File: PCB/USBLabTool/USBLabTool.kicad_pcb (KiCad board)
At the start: 2 copper layers, 228 parts, among them J1 Conn_01x06_Pin, J10 T_pwm, J11 T_buf, J12 T_buf, J13 ADC2, J14 ADC1, J15 +3.3VA, J16 +3.3VA, J17 2x01, J19 T_N5V, J2 Conn_02x12_Odd_Even, J20 USB_C_Receptacle, J3 T_att, J4 T_att, J5 T_acdc, J6 T_acdc, J7 T_amp, J8 T_amp, J9 T_pwm, K1 G5V-2, K2 G5V-2, SW1 SW_Push, U1 AQY284SX, U10 Opamp_Quad, U11 DG403, U12 STM32H562VGTx, U13 r1283, U14 ST1L05APU33R, U15 ST1L05APU33R, U16 LTC1983ES6-5#TRPBF, U17 TCPP01-M12, U18 74HC245, U2 AQY284SX, U20 74HC245, U3 CD74HC4316M96, U4 LMP7718, U5 CD74HC4316M96, U6 LMP7718, U7 OPA863, U8 OPA863, U9 Opamp_Quad, Y1 32.768kHz

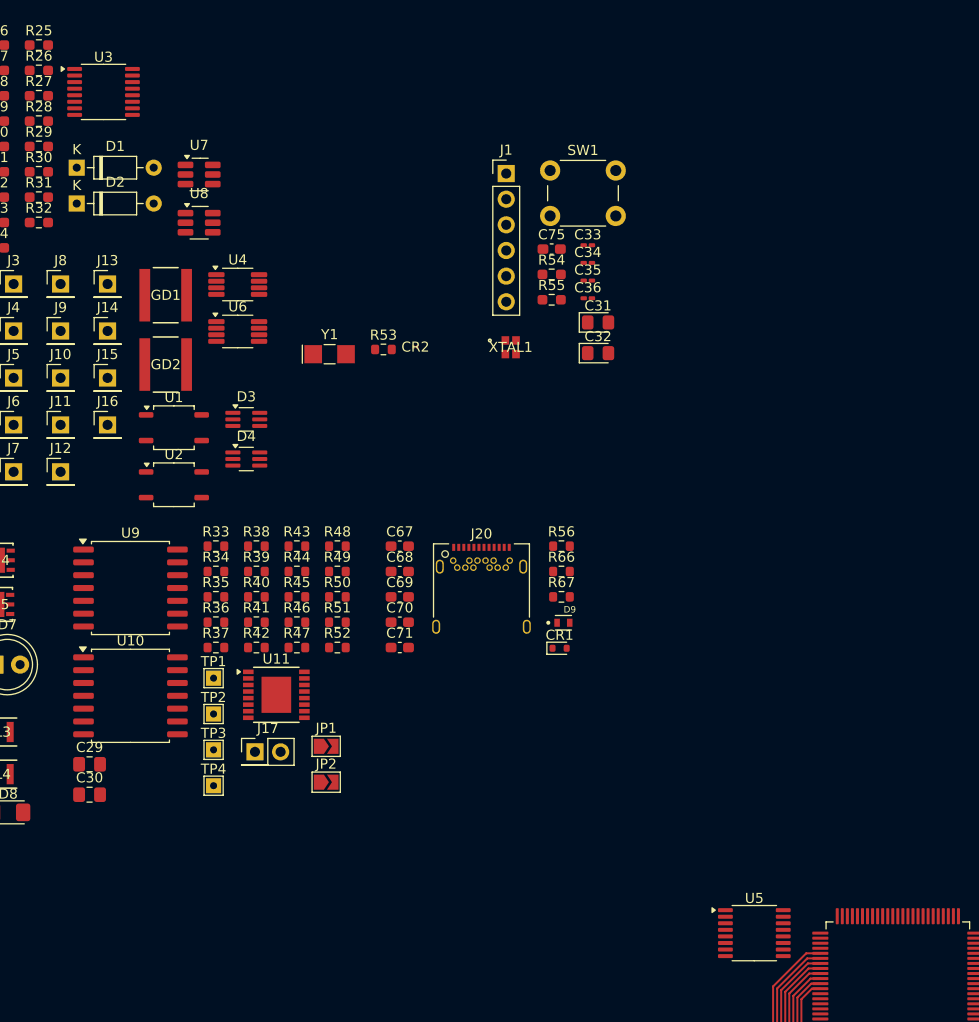
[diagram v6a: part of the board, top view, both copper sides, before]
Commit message: swap MCU  pins for routing
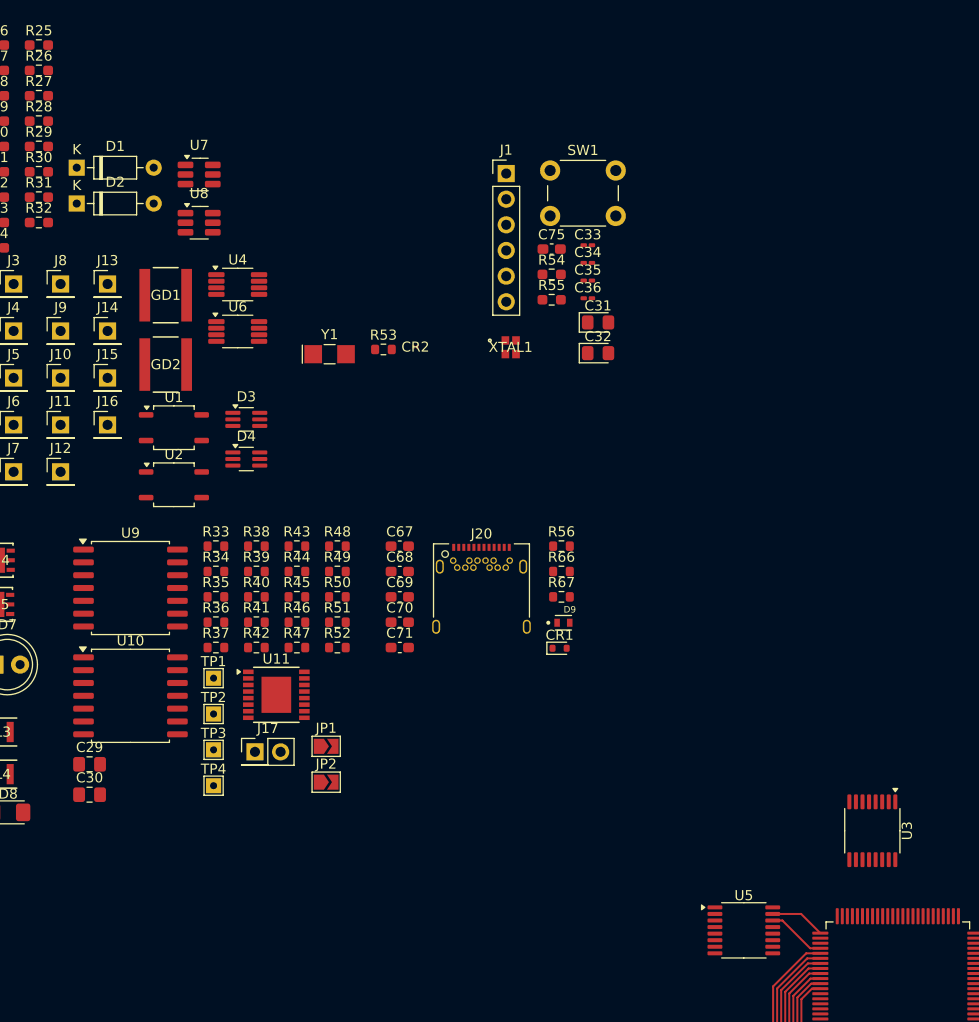
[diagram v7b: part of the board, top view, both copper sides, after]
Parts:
- U3, U5: value CD74HC4316M96 -> CD74HC4316PWR
- moved U3 105.6 mm to (140.6, 105.3), turned to -90 degrees
- moved U5 1.07 mm to (127.9, 115.2)
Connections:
- U12 pad 35: CH1_amp_10 -> CH1_amp_1
- U12 pad 47: CH1_amp_1 -> CH1_amp_10
- U12 pad 51: CH0_amp_10 -> CH0_amp_1
- U12 pad 54: CH0_amp_1 -> CH0_amp_10
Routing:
- net CH0_amp_10: track 0.00 -> 5.85 mm
- net CH0_amp_1: track 0.00 -> 5.50 mm
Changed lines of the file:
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@@
 			(layers "F.Cu" "F.Paste" "F.Mask")
 			(roundrect_rratio 0.25)
-			(net 139 "CH1_amp_10")
+			(net 141 "CH1_amp_1")
 			(pinfunction "PB0")
 			(pintype "bidirectional")
@@
 			(layers "F.Cu" "F.Paste" "F.Mask")
 			(roundrect_rratio 0.25)
-			(net 141 "CH1_amp_1")
+			(net 139 "CH1_amp_10")
 			(pinfunction "PB10")
 			(pintype "bidirectional")
@@
 			(layers "F.Cu" "F.Paste" "F.Mask")
 			(roundrect_rratio 0.25)
-			(net 146 "CH0_amp_10")
+			(net 143 "CH0_amp_1")
 			(pinfunction "PB12")
 			(pintype "bidirectional")
@@
 			(layers "F.Cu" "F.Paste" "F.Mask")
 			(roundrect_rratio 0.25)
-			(net 143 "CH0_amp_1")
+			(net 146 "CH0_amp_10")
 			(pinfunction "PB15")
 			(pintype "bidirectional")
@@
 	(footprint "Package_SO:TSSOP-16_4.4x5mm_P0.65mm"
 		(layer "F.Cu")
-		(at 128.9375 115.475)
+		(at 127.9 115.2)
 		(descr "TSSOP, 16 Pin (https://www.jedec.org/document_search?search_api_views_fulltext=MO-153), generated with kicad-footprint-generator ipc_gullwing_generator.py")
 		(tags "TSSOP SO JEDEC-MO-153-AB TI-PW0016A Microchip-ST Toshiba-TSSOP16-P-0044-0.65A NXP-SOT403-1 Infineon-P-TSSOP-16-800")
@@
 			)
 		)
-		(property "Value" "CD74HC4316M96"
+		(property "Value" "CD74HC4316PWR"
 			(at 0 3.45 0)
 			(layer "F.Fab")
@@
 			)
 		)
-		(property "Datasheet" "https://www.digikey.com/en/products/detail/texas-instruments/CD74HC4316M96/555784"
+		(property "Datasheet" "https://www.digikey.com/en/products/detail/texas-instruments/CD74HC4316PWR/1507290"
 			(at 0 0 0)
 			(layer "F.Fab")
@@
 		(fp_text user "*"
 			(at -2.4638 -0.75 0)
-			(unlocked yes)
 			(layer "F.SilkS")
 			(effects
@@
 		(fp_text user "*"
 			(at -2.4638 -0.75 0)
+			(unlocked yes)
 			(layer "F.SilkS")
 			(effects
@@
 		(fp_text user "*"
 			(at -1.016 -0.75 0)
+			(unlocked yes)
 			(layer "F.Fab")
 			(effects
@@
 		(fp_text user "*"
 			(at -1.016 -0.75 0)
-			(unlocked yes)
 			(layer "F.Fab")
 			(effects
@@
 	(footprint "Package_SO:TSSOP-16_4.4x5mm_P0.65mm"
 		(layer "F.Cu")
-		(at 64.49 32.175)
+		(at 140.625 105.3375 -90)
 		(descr "TSSOP, 16 Pin (https://www.jedec.org/document_search?search_api_views_fulltext=MO-153), generated with kicad-footprint-generator ipc_gullwing_generator.py")
 		(tags "TSSOP SO JEDEC-MO-153-AB TI-PW0016A Microchip-ST Toshiba-TSSOP16-P-0044-0.65A NXP-SOT403-1 Infineon-P-TSSOP-16-800")
 		(property "Reference" "U3"
-			(at 0 -3.45 0)
+			(at 0 -3.45 90)
 			(layer "F.SilkS")
 			(effects
@@
 			)
 		)
-		(property "Value" "CD74HC4316M96"
-			(at 0 3.45 0)
+		(property "Value" "CD74HC4316PWR"
+			(at 0 3.45 90)
 			(layer "F.Fab")
 			(effects
@@
 		)
 		(property "Footprint" "Package_SO:TSSOP-16_4.4x5mm_P0.65mm"
-			(at 0 0 0)
+			(at 0 0 90)
 			(layer "F.Fab")
 			(hide yes)
@@
 			)
 		)
-		(property "Datasheet" "https://www.digikey.com/en/products/detail/texas-instruments/CD74HC4316M96/555784"
-			(at 0 0 0)
+		(property "Datasheet" "https://www.digikey.com/en/products/detail/texas-instruments/CD74HC4316PWR/1507290"
+			(at 0 0 90)
 			(layer "F.Fab")
 			(hide yes)
@@
 		)
 		(property "Description" ""
-			(at 0 0 0)
+			(at 0 0 90)
 			(layer "F.Fab")
 			(hide yes)
@@
 		(attr smd)
 		(fp_line
-			(start 0 -2.735)
-			(end -2.2 -2.735)
+			(start 0 2.735)
+			(end -2.2 2.735)
 			(stroke
 				(width 0.12)
@@
 		)
 		(fp_line
-			(start 0 -2.735)
-			(end 2.2 -2.735)
+			(start 0 2.735)
+			(end 2.2 2.735)
 			(stroke
 				(width 0.12)
@@
 		)
 		(fp_line
-			(start 0 2.735)
-			(end -2.2 2.735)
+			(start 0 -2.735)
+			(end -2.2 -2.735)
 			(stroke
 				(width 0.12)
@@
 		)
 		(fp_line
-			(start 0 2.735)
-			(end 2.2 2.735)
+			(start 0 -2.735)
+			(end 2.2 -2.735)
 			(stroke
 				(width 0.12)
@@
 		)
 		(fp_line
-			(start -3.85 -2.75)
-			(end -3.85 2.75)
+			(start -3.85 2.75)
+			(end 3.85 2.75)
 			(stroke
 				(width 0.05)
@@
 		)
 		(fp_line
-			(start -3.85 2.75)
-			(end 3.85 2.75)
+			(start 3.85 2.75)
+			(end 3.85 -2.75)
 			(stroke
 				(width 0.05)
@@
 		)
 		(fp_line
-			(start 3.85 -2.75)
-			(end -3.85 -2.75)
+			(start -3.85 -2.75)
+			(end -3.85 2.75)
 			(stroke
 				(width 0.05)
@@
 		)
 		(fp_line
-			(start 3.85 2.75)
-			(end 3.85 -2.75)
+			(start 3.85 -2.75)
+			(end -3.85 -2.75)
 			(stroke
 				(width 0.05)
@@
 		)
 		(fp_line
-			(start -2.2 -1.5)
-			(end -1.2 -2.5)
+			(start -2.2 2.5)
+			(end -2.2 -1.5)
 			(stroke
 				(width 0.1)
@@
 		)
 		(fp_line
-			(start -2.2 2.5)
-			(end -2.2 -1.5)
+			(start 2.2 2.5)
+			(end -2.2 2.5)
 			(stroke
 				(width 0.1)
@@
 		)
 		(fp_line
-			(start -1.2 -2.5)
-			(end 2.2 -2.5)
+			(start -2.2 -1.5)
+			(end -1.2 -2.5)
 			(stroke
 				(width 0.1)
@@
 		)
 		(fp_line
-			(start 2.2 -2.5)
-			(end 2.2 2.5)
+			(start -1.2 -2.5)
+			(end 2.2 -2.5)
 			(stroke
 				(width 0.1)
@@
 		)
 		(fp_line
-			(start 2.2 2.5)
-			(end -2.2 2.5)
+			(start 2.2 -2.5)
+			(end 2.2 2.5)
 			(stroke
 				(width 0.1)
@@
 		)
 		(fp_text user "${REFERENCE}"
-			(at 0 0 0)
+			(at 0 0 90)
 			(layer "F.Fab")
 			(effects
@@
 		)
 		(pad "1" smd roundrect
-			(at -2.8625 -2.275)
+			(at -2.8625 -2.275 270)
 			(size 1.475 0.4)
 			(layers "F.Cu" "F.Paste" "F.Mask")
@@
 		)
 		(pad "2" smd roundrect
-			(at -2.8625 -1.625)
+			(at -2.8625 -1.625 270)
 			(size 1.475 0.4)
 			(layers "F.Cu" "F.Paste" "F.Mask")
@@
 		)
 		(pad "3" smd roundrect
-			(at -2.8625 -0.975)
+			(at -2.8625 -0.975 270)
 			(size 1.475 0.4)
 			(layers "F.Cu" "F.Paste" "F.Mask")
@@
 		)
 		(pad "4" smd roundrect
-			(at -2.8625 -0.325)
+			(at -2.8625 -0.325 270)
 			(size 1.475 0.4)
 			(layers "F.Cu" "F.Paste" "F.Mask")
@@
 		)
 		(pad "5" smd roundrect
-			(at -2.8625 0.325)
+			(at -2.8625 0.325 270)
 			(size 1.475 0.4)
 			(layers "F.Cu" "F.Paste" "F.Mask")
@@
 		)
 		(pad "6" smd roundrect
-			(at -2.8625 0.975)
+			(at -2.8625 0.975 270)
 			(size 1.475 0.4)
 			(layers "F.Cu" "F.Paste" "F.Mask")
@@
 		)
 		(pad "7" smd roundrect
-			(at -2.8625 1.625)
+			(at -2.8625 1.625 270)
 			(size 1.475 0.4)
 			(layers "F.Cu" "F.Paste" "F.Mask")
@@
 		)
 		(pad "8" smd roundrect
-			(at -2.8625 2.275)
+			(at -2.8625 2.275 270)
 			(size 1.475 0.4)
 			(layers "F.Cu" "F.Paste" "F.Mask")
@@
 		)
 		(pad "9" smd roundrect
-			(at 2.8625 2.275)
+			(at 2.8625 2.275 270)
 			(size 1.475 0.4)
 			(layers "F.Cu" "F.Paste" "F.Mask")
@@
 		)
 		(pad "10" smd roundrect
-			(at 2.8625 1.625)
+			(at 2.8625 1.625 270)
 			(size 1.475 0.4)
 			(layers "F.Cu" "F.Paste" "F.Mask")
@@
 		)
 		(pad "11" smd roundrect
-			(at 2.8625 0.975)
+			(at 2.8625 0.975 270)
 			(size 1.475 0.4)
 			(layers "F.Cu" "F.Paste" "F.Mask")
@@
 		)
 		(pad "12" smd roundrect
-			(at 2.8625 0.325)
+			(at 2.8625 0.325 270)
 			(size 1.475 0.4)
 			(layers "F.Cu" "F.Paste" "F.Mask")
@@
 		)
 		(pad "13" smd roundrect
-			(at 2.8625 -0.325)
+			(at 2.8625 -0.325 270)
 			(size 1.475 0.4)
 			(layers "F.Cu" "F.Paste" "F.Mask")
@@
 		)
 		(pad "14" smd roundrect
-			(at 2.8625 -0.975)
+			(at 2.8625 -0.975 270)
 			(size 1.475 0.4)
 			(layers "F.Cu" "F.Paste" "F.Mask")
@@
 		)
 		(pad "15" smd roundrect
-			(at 2.8625 -1.625)
+			(at 2.8625 -1.625 270)
 			(size 1.475 0.4)
 			(layers "F.Cu" "F.Paste" "F.Mask")
@@
 		)
 		(pad "16" smd roundrect
-			(at 2.8625 -2.275)
+			(at 2.8625 -2.275 270)
 			(size 1.475 0.4)
 			(layers "F.Cu" "F.Paste" "F.Mask")
@@
 	)
 	(segment
+		(start 130.7625 113.575)
+		(end 133.575 113.575)
+		(width 0.2)
+		(layer "F.Cu")
+		(net 143)
+	)
+	(segment
+		(start 133.575 113.575)
+		(end 135.475 115.475)
+		(width 0.2)
+		(layer "F.Cu")
+		(net 143)
+	)
+	(segment
+		(start 134.468456 116.975)
+		(end 135.475 116.975)
+		(width 0.2)
+		(layer "F.Cu")
+		(net 146)
+	)
+	(segment
+		(start 130.7625 114.225)
+		(end 131.718456 114.225)
+		(width 0.2)
+		(layer "F.Cu")
+		(net 146)
+	)
+	(segment
+		(start 131.718456 114.225)
+		(end 134.468456 116.975)
+		(width 0.2)
+		(layer "F.Cu")
+		(net 146)
+	)
+	(segment

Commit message: starting the layout again
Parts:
- moved C19 179.0 mm to (207.2, 93.3)
- moved C28 176.6 mm to (219.2, 57.3)
- moved C22 176.4 mm to (216.8, 43.9)
- moved L1 175.3 mm to (207.2, 96.7)
- moved C11 172.0 mm to (192.9, 101.2)
- moved C20 170.7 mm to (208.2, 63.0)
- moved R25 169.3 mm to (215.6, 89.7)
- moved R28 166.2 mm to (215.6, 88.0)
- moved R31 165.6 mm to (215.0, 95.5)
- moved C14 165.6 mm to (188.6, 102.7)
- moved C15 165.6 mm to (188.6, 105.2)
- moved R32 164.5 mm to (221.6, 62.6)
- moved C76 164.2 mm to (69.7, 29.3)
- moved R57 164.2 mm to (69.7, 34.4)
- moved R65 164.2 mm to (69.7, 36.9)
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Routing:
- net CH0_amp_10: track 5.85 -> 0.00 mm
- net CH0_amp_1: track 5.50 -> 0.00 mm
